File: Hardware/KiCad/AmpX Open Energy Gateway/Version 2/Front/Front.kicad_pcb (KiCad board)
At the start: 2 copper layers, 42.5 x 32 mm, 11 parts, among them J3 Status Conn Top

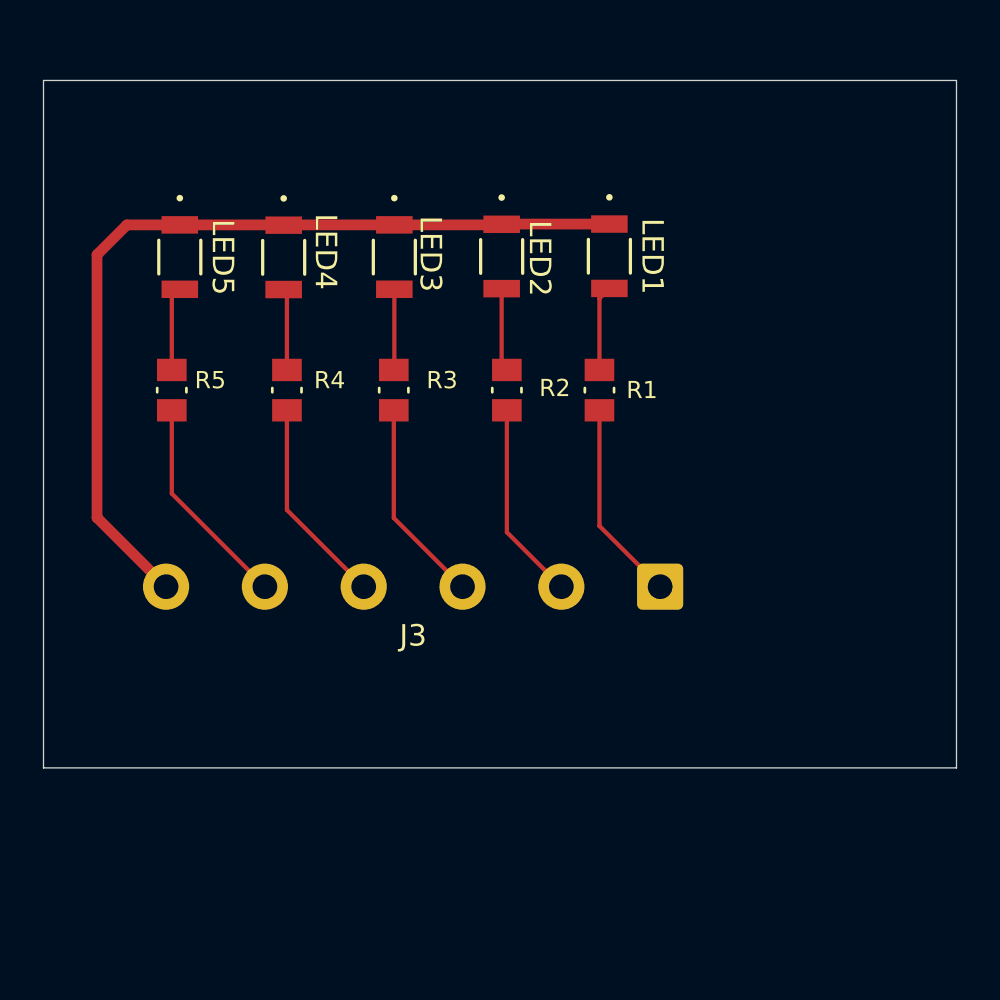
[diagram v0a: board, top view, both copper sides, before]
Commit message: added extra wire for ground
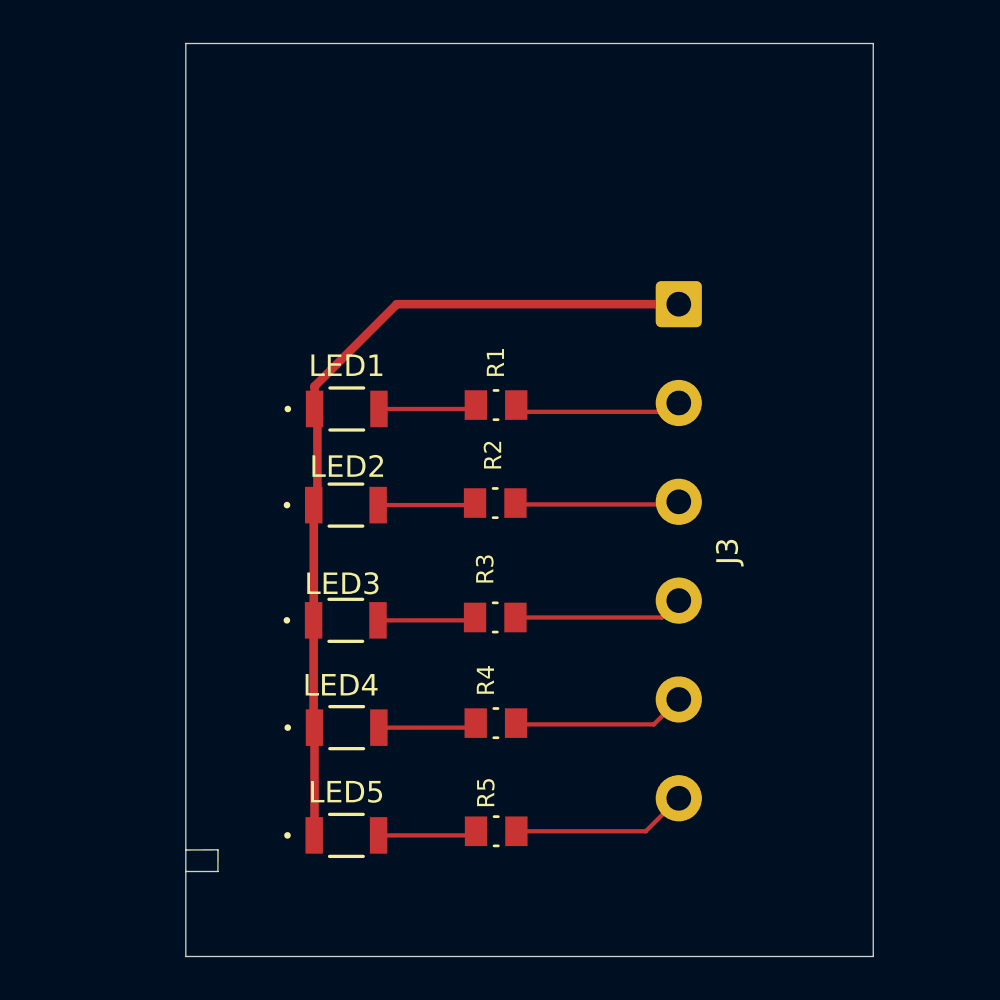
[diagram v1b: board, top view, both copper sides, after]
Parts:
- moved LED5 28.0 mm to (137.6, 111.8), turned to 0 degrees
- moved R5 25.5 mm to (144.6, 111.6), turned to 0 degrees
- moved LED4 22.1 mm to (137.6, 106.8), turned to 0 degrees
- moved R4 18.3 mm to (144.6, 106.6), turned to 0 degrees
- moved LED3 17.1 mm to (137.6, 101.8), turned to 0 degrees
- moved LED1 14.1 mm to (137.6, 91.9), turned to 0 degrees
- moved LED2 13.7 mm to (137.6, 96.4), turned to 0 degrees
- moved J3 13.2 mm to (153.1, 87.0), turned to -90 degrees
- moved R3 11.6 mm to (144.5, 101.6), turned to 0 degrees
- moved R2 5.28 mm to (144.5, 96.3), turned to 0 degrees
- moved R1 4.86 mm to (144.6, 91.7), turned to 0 degrees
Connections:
- LED1 pad 1: Net-(J3-Pin_6) -> Net-(J3-Pin_1)
- LED2 pad 1: Net-(J3-Pin_6) -> Net-(J3-Pin_1)
- LED3 pad 1: Net-(J3-Pin_6) -> Net-(J3-Pin_1)
- LED4 pad 1: Net-(J3-Pin_6) -> Net-(J3-Pin_1)
- LED5 pad 1: Net-(J3-Pin_6) -> Net-(J3-Pin_1)
- R1 pad 2: Net-(J3-Pin_1) -> Net-(J3-Pin_2)
- R2 pad 2: Net-(J3-Pin_2) -> Net-(J3-Pin_3)
- R3 pad 2: Net-(J3-Pin_3) -> Net-(J3-Pin_4)
- R4 pad 2: Net-(J3-Pin_4) -> Net-(J3-Pin_5)
- R5 pad 2: Net-(J3-Pin_5) -> Net-(J3-Pin_6)
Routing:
- net Net-(J3-Pin_6): track 41.3 -> 8.20 mm
- net Net-(J3-Pin_1): track 9.38 -> 39.7 mm
- net Net-(J3-Pin_5): track 10.0 -> 7.69 mm
- net Net-(J3-Pin_3): track 9.53 -> 7.31 mm
- net Net-(J3-Pin_4): track 10.6 -> 8.45 mm
- net Net-(J3-Pin_2): track 9.26 -> 7.38 mm
- net Net-(LED2-Pad2): track 3.88 -> 4.89 mm
- net Net-(LED4-Pad2): track 4.07 -> 5.07 mm
- net Net-(LED3-Pad2): track 3.77 -> 4.61 mm
- net Net-(LED5-Pad2): track 4.06 -> 4.76 mm
- net Net-(LED1-Pad2): track 4.09 -> 4.69 mm
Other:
- board size 42.5 x 32 mm -> 32 x 42.5 mm
